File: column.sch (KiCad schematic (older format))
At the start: 15 parts

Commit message: Place parts
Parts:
- gave numbers to parts that had none: 7

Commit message: Layout half done
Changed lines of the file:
@@
 $Descr A4 11693 8268
 encoding utf-8
-Sheet 16 17
+Sheet 4 17
 Title ""
 Date ""
@@
 AR Path="/5FA2E67E/5F7BAC96" Ref="D?"  Part="1"
 AR Path="/5FA2E6B0/5F7BAC96" Ref="D?"  Part="1"
-F 0 "D1" H 2293 2195 50  0000 C CNN
+F 0 "D181" H 2293 2195 50  0000 C CNN
 F 1 "LED" H 2293 2286 50  0000 C CNN
 F 2 "LED_SMD:LED_0402_1005Metric" H 2300 2450 50  0001 C CNN
@@
 AR Path="/5FA2E67E/5F7BB35F" Ref="D?"  Part="1"
 AR Path="/5FA2E6B0/5F7BB35F" Ref="D?"  Part="1"
-F 0 "D2" H 2293 2545 50  0000 C CNN
+F 0 "D182" H 2293 2545 50  0000 C CNN
 F 1 "LED" H 2293 2636 50  0000 C CNN
 F 2 "LED_SMD:LED_0402_1005Metric" H 2300 2800 50  0001 C CNN
@@
 AR Path="/5FA2E67E/5F7BBBBA" Ref="D?"  Part="1"
 AR Path="/5FA2E6B0/5F7BBBBA" Ref="D?"  Part="1"
-F 0 "D3" H 2293 2895 50  0000 C CNN
+F 0 "D183" H 2293 2895 50  0000 C CNN
 F 1 "LED" H 2293 2986 50  0000 C CNN
 F 2 "LED_SMD:LED_0402_1005Metric" H 2300 3150 50  0001 C CNN
@@
 AR Path="/5FA2E67E/5F7BBBC1" Ref="D?"  Part="1"
 AR Path="/5FA2E6B0/5F7BBBC1" Ref="D?"  Part="1"
-F 0 "D4" H 2293 3245 50  0000 C CNN
+F 0 "D184" H 2293 3245 50  0000 C CNN
 F 1 "LED" H 2293 3336 50  0000 C CNN
 F 2 "LED_SMD:LED_0402_1005Metric" H 2300 3500 50  0001 C CNN
@@
 AR Path="/5FA2E67E/5F7BC4EE" Ref="D?"  Part="1"
 AR Path="/5FA2E6B0/5F7BC4EE" Ref="D?"  Part="1"
-F 0 "D5" H 2293 3595 50  0000 C CNN
+F 0 "D185" H 2293 3595 50  0000 C CNN
 F 1 "LED" H 2293 3686 50  0000 C CNN
 F 2 "LED_SMD:LED_0402_1005Metric" H 2300 3850 50  0001 C CNN
@@
 AR Path="/5FA2E67E/5F7BC4F5" Ref="D?"  Part="1"
 AR Path="/5FA2E6B0/5F7BC4F5" Ref="D?"  Part="1"
-F 0 "D6" H 2293 3945 50  0000 C CNN
+F 0 "D186" H 2293 3945 50  0000 C CNN
 F 1 "LED" H 2293 4036 50  0000 C CNN
 F 2 "LED_SMD:LED_0402_1005Metric" H 2300 4200 50  0001 C CNN
@@
 AR Path="/5FA2E67E/5F7BC4FC" Ref="D?"  Part="1"
 AR Path="/5FA2E6B0/5F7BC4FC" Ref="D?"  Part="1"
-F 0 "D7" H 2293 4295 50  0000 C CNN
+F 0 "D187" H 2293 4295 50  0000 C CNN
 F 1 "LED" H 2293 4386 50  0000 C CNN
 F 2 "LED_SMD:LED_0402_1005Metric" H 2300 4550 50  0001 C CNN
@@
 AR Path="/5FA2E67E/5F7BC503" Ref="D?"  Part="1"
 AR Path="/5FA2E6B0/5F7BC503" Ref="D?"  Part="1"
-F 0 "D8" H 2293 4645 50  0000 C CNN
+F 0 "D188" H 2293 4645 50  0000 C CNN
 F 1 "LED" H 2293 4736 50  0000 C CNN
 F 2 "LED_SMD:LED_0402_1005Metric" H 2300 4900 50  0001 C CNN
@@
 AR Path="/5FA2E67E/5F92EDB7" Ref="D?"  Part="1"
 AR Path="/5FA2E6B0/5F92EDB7" Ref="D?"  Part="1"
-F 0 "D9" H 3193 2195 50  0000 C CNN
+F 0 "D189" H 3193 2195 50  0000 C CNN
 F 1 "LED" H 3193 2286 50  0000 C CNN
 F 2 "LED_SMD:LED_0402_1005Metric" H 3200 2450 50  0001 C CNN
@@
 AR Path="/5FA2E67E/5F92EDBE" Ref="D?"  Part="1"
 AR Path="/5FA2E6B0/5F92EDBE" Ref="D?"  Part="1"
-F 0 "D10" H 3193 2545 50  0000 C CNN
+F 0 "D190" H 3193 2545 50  0000 C CNN
 F 1 "LED" H 3193 2636 50  0000 C CNN
 F 2 "LED_SMD:LED_0402_1005Metric" H 3200 2800 50  0001 C CNN
@@
 AR Path="/5FA2E67E/5F92EDC5" Ref="D?"  Part="1"
 AR Path="/5FA2E6B0/5F92EDC5" Ref="D?"  Part="1"
-F 0 "D11" H 3193 2895 50  0000 C CNN
+F 0 "D191" H 3193 2895 50  0000 C CNN
 F 1 "LED" H 3193 2986 50  0000 C CNN
 F 2 "LED_SMD:LED_0402_1005Metric" H 3200 3150 50  0001 C CNN
@@
 AR Path="/5FA2E67E/5F92EDCC" Ref="D?"  Part="1"
 AR Path="/5FA2E6B0/5F92EDCC" Ref="D?"  Part="1"
-F 0 "D12" H 3193 3245 50  0000 C CNN
+F 0 "D192" H 3193 3245 50  0000 C CNN
 F 1 "LED" H 3193 3336 50  0000 C CNN
 F 2 "LED_SMD:LED_0402_1005Metric" H 3200 3500 50  0001 C CNN
@@
 AR Path="/5FA2E67E/5F92EDD3" Ref="D?"  Part="1"
 AR Path="/5FA2E6B0/5F92EDD3" Ref="D?"  Part="1"
-F 0 "D13" H 3193 3595 50  0000 C CNN
+F 0 "D193" H 3193 3595 50  0000 C CNN
 F 1 "LED" H 3193 3686 50  0000 C CNN
 F 2 "LED_SMD:LED_0402_1005Metric" H 3200 3850 50  0001 C CNN
@@
 AR Path="/5FA2E67E/5F92EDDA" Ref="D?"  Part="1"
 AR Path="/5FA2E6B0/5F92EDDA" Ref="D?"  Part="1"
-F 0 "D14" H 3193 3945 50  0000 C CNN
+F 0 "D194" H 3193 3945 50  0000 C CNN
 F 1 "LED" H 3193 4036 50  0000 C CNN
 F 2 "LED_SMD:LED_0402_1005Metric" H 3200 4200 50  0001 C CNN
@@
 AR Path="/5FA2E67E/5F92EDE1" Ref="D?"  Part="1"
 AR Path="/5FA2E6B0/5F92EDE1" Ref="D?"  Part="1"
-F 0 "D15" H 3193 4295 50  0000 C CNN
+F 0 "D195" H 3193 4295 50  0000 C CNN
 F 1 "LED" H 3193 4386 50  0000 C CNN
 F 2 "LED_SMD:LED_0402_1005Metric" H 3200 4550 50  0001 C CNN

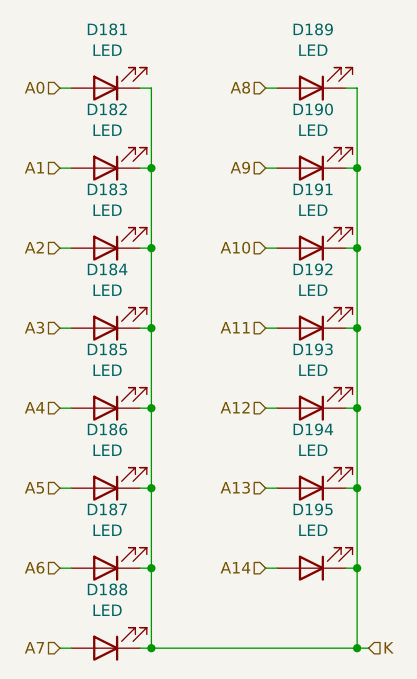
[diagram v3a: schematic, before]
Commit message: Bump up charge current to 45mA
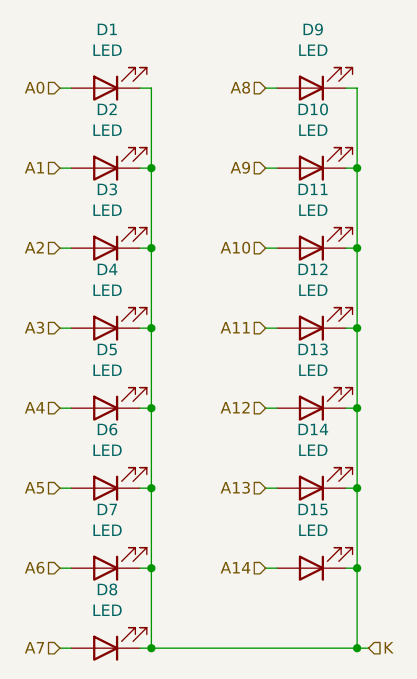
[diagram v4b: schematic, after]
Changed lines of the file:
@@
 AR Path="/5FA2E67E/5F7BAC96" Ref="D?"  Part="1"
 AR Path="/5FA2E6B0/5F7BAC96" Ref="D?"  Part="1"
-F 0 "D181" H 2293 2195 50  0000 C CNN
+F 0 "D1" H 2293 2195 50  0000 C CNN
 F 1 "LED" H 2293 2286 50  0000 C CNN
 F 2 "LED_SMD:LED_0402_1005Metric" H 2300 2450 50  0001 C CNN
@@
 AR Path="/5FA2E67E/5F7BB35F" Ref="D?"  Part="1"
 AR Path="/5FA2E6B0/5F7BB35F" Ref="D?"  Part="1"
-F 0 "D182" H 2293 2545 50  0000 C CNN
+F 0 "D2" H 2293 2545 50  0000 C CNN
 F 1 "LED" H 2293 2636 50  0000 C CNN
 F 2 "LED_SMD:LED_0402_1005Metric" H 2300 2800 50  0001 C CNN
@@
 AR Path="/5FA2E67E/5F7BBBBA" Ref="D?"  Part="1"
 AR Path="/5FA2E6B0/5F7BBBBA" Ref="D?"  Part="1"
-F 0 "D183" H 2293 2895 50  0000 C CNN
+F 0 "D3" H 2293 2895 50  0000 C CNN
 F 1 "LED" H 2293 2986 50  0000 C CNN
 F 2 "LED_SMD:LED_0402_1005Metric" H 2300 3150 50  0001 C CNN
@@
 AR Path="/5FA2E67E/5F7BBBC1" Ref="D?"  Part="1"
 AR Path="/5FA2E6B0/5F7BBBC1" Ref="D?"  Part="1"
-F 0 "D184" H 2293 3245 50  0000 C CNN
+F 0 "D4" H 2293 3245 50  0000 C CNN
 F 1 "LED" H 2293 3336 50  0000 C CNN
 F 2 "LED_SMD:LED_0402_1005Metric" H 2300 3500 50  0001 C CNN
@@
 AR Path="/5FA2E67E/5F7BC4EE" Ref="D?"  Part="1"
 AR Path="/5FA2E6B0/5F7BC4EE" Ref="D?"  Part="1"
-F 0 "D185" H 2293 3595 50  0000 C CNN
+F 0 "D5" H 2293 3595 50  0000 C CNN
 F 1 "LED" H 2293 3686 50  0000 C CNN
 F 2 "LED_SMD:LED_0402_1005Metric" H 2300 3850 50  0001 C CNN
@@
 AR Path="/5FA2E67E/5F7BC4F5" Ref="D?"  Part="1"
 AR Path="/5FA2E6B0/5F7BC4F5" Ref="D?"  Part="1"
-F 0 "D186" H 2293 3945 50  0000 C CNN
+F 0 "D6" H 2293 3945 50  0000 C CNN
 F 1 "LED" H 2293 4036 50  0000 C CNN
 F 2 "LED_SMD:LED_0402_1005Metric" H 2300 4200 50  0001 C CNN
@@
 AR Path="/5FA2E67E/5F7BC4FC" Ref="D?"  Part="1"
 AR Path="/5FA2E6B0/5F7BC4FC" Ref="D?"  Part="1"
-F 0 "D187" H 2293 4295 50  0000 C CNN
+F 0 "D7" H 2293 4295 50  0000 C CNN
 F 1 "LED" H 2293 4386 50  0000 C CNN
 F 2 "LED_SMD:LED_0402_1005Metric" H 2300 4550 50  0001 C CNN
@@
 AR Path="/5FA2E67E/5F7BC503" Ref="D?"  Part="1"
 AR Path="/5FA2E6B0/5F7BC503" Ref="D?"  Part="1"
-F 0 "D188" H 2293 4645 50  0000 C CNN
+F 0 "D8" H 2293 4645 50  0000 C CNN
 F 1 "LED" H 2293 4736 50  0000 C CNN
 F 2 "LED_SMD:LED_0402_1005Metric" H 2300 4900 50  0001 C CNN
@@
 AR Path="/5FA2E67E/5F92EDB7" Ref="D?"  Part="1"
 AR Path="/5FA2E6B0/5F92EDB7" Ref="D?"  Part="1"
-F 0 "D189" H 3193 2195 50  0000 C CNN
+F 0 "D9" H 3193 2195 50  0000 C CNN
 F 1 "LED" H 3193 2286 50  0000 C CNN
 F 2 "LED_SMD:LED_0402_1005Metric" H 3200 2450 50  0001 C CNN
@@
 AR Path="/5FA2E67E/5F92EDBE" Ref="D?"  Part="1"
 AR Path="/5FA2E6B0/5F92EDBE" Ref="D?"  Part="1"
-F 0 "D190" H 3193 2545 50  0000 C CNN
+F 0 "D10" H 3193 2545 50  0000 C CNN
 F 1 "LED" H 3193 2636 50  0000 C CNN
 F 2 "LED_SMD:LED_0402_1005Metric" H 3200 2800 50  0001 C CNN
@@
 AR Path="/5FA2E67E/5F92EDC5" Ref="D?"  Part="1"
 AR Path="/5FA2E6B0/5F92EDC5" Ref="D?"  Part="1"
-F 0 "D191" H 3193 2895 50  0000 C CNN
+F 0 "D11" H 3193 2895 50  0000 C CNN
 F 1 "LED" H 3193 2986 50  0000 C CNN
 F 2 "LED_SMD:LED_0402_1005Metric" H 3200 3150 50  0001 C CNN
@@
 AR Path="/5FA2E67E/5F92EDCC" Ref="D?"  Part="1"
 AR Path="/5FA2E6B0/5F92EDCC" Ref="D?"  Part="1"
-F 0 "D192" H 3193 3245 50  0000 C CNN
+F 0 "D12" H 3193 3245 50  0000 C CNN
 F 1 "LED" H 3193 3336 50  0000 C CNN
 F 2 "LED_SMD:LED_0402_1005Metric" H 3200 3500 50  0001 C CNN
@@
 AR Path="/5FA2E67E/5F92EDD3" Ref="D?"  Part="1"
 AR Path="/5FA2E6B0/5F92EDD3" Ref="D?"  Part="1"
-F 0 "D193" H 3193 3595 50  0000 C CNN
+F 0 "D13" H 3193 3595 50  0000 C CNN
 F 1 "LED" H 3193 3686 50  0000 C CNN
 F 2 "LED_SMD:LED_0402_1005Metric" H 3200 3850 50  0001 C CNN
@@
 AR Path="/5FA2E67E/5F92EDDA" Ref="D?"  Part="1"
 AR Path="/5FA2E6B0/5F92EDDA" Ref="D?"  Part="1"
-F 0 "D194" H 3193 3945 50  0000 C CNN
+F 0 "D14" H 3193 3945 50  0000 C CNN
 F 1 "LED" H 3193 4036 50  0000 C CNN
 F 2 "LED_SMD:LED_0402_1005Metric" H 3200 4200 50  0001 C CNN
@@
 AR Path="/5FA2E67E/5F92EDE1" Ref="D?"  Part="1"
 AR Path="/5FA2E6B0/5F92EDE1" Ref="D?"  Part="1"
-F 0 "D195" H 3193 4295 50  0000 C CNN
+F 0 "D15" H 3193 4295 50  0000 C CNN
 F 1 "LED" H 3193 4386 50  0000 C CNN
 F 2 "LED_SMD:LED_0402_1005Metric" H 3200 4550 50  0001 C CNN
